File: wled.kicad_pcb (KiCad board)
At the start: 2 copper layers, 61.5 x 28.4 mm, 20 parts, among them J1 PROGRAM_HEADER, J2 LED0, J3 QWIIC, J4 POWER, U1 ESP-12F, U2 AMS1117-3.3

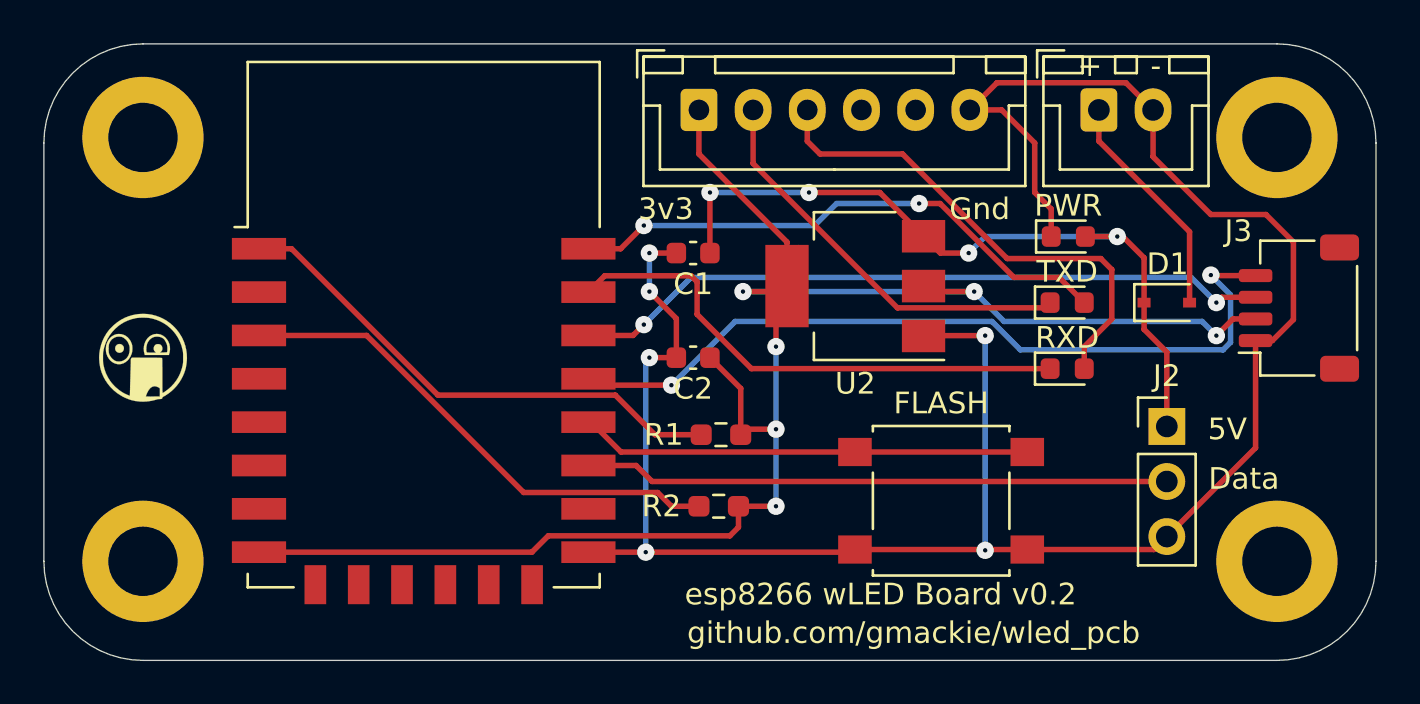
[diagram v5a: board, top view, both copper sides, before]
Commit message: v0.3 (fix LEDs and add reset SW)
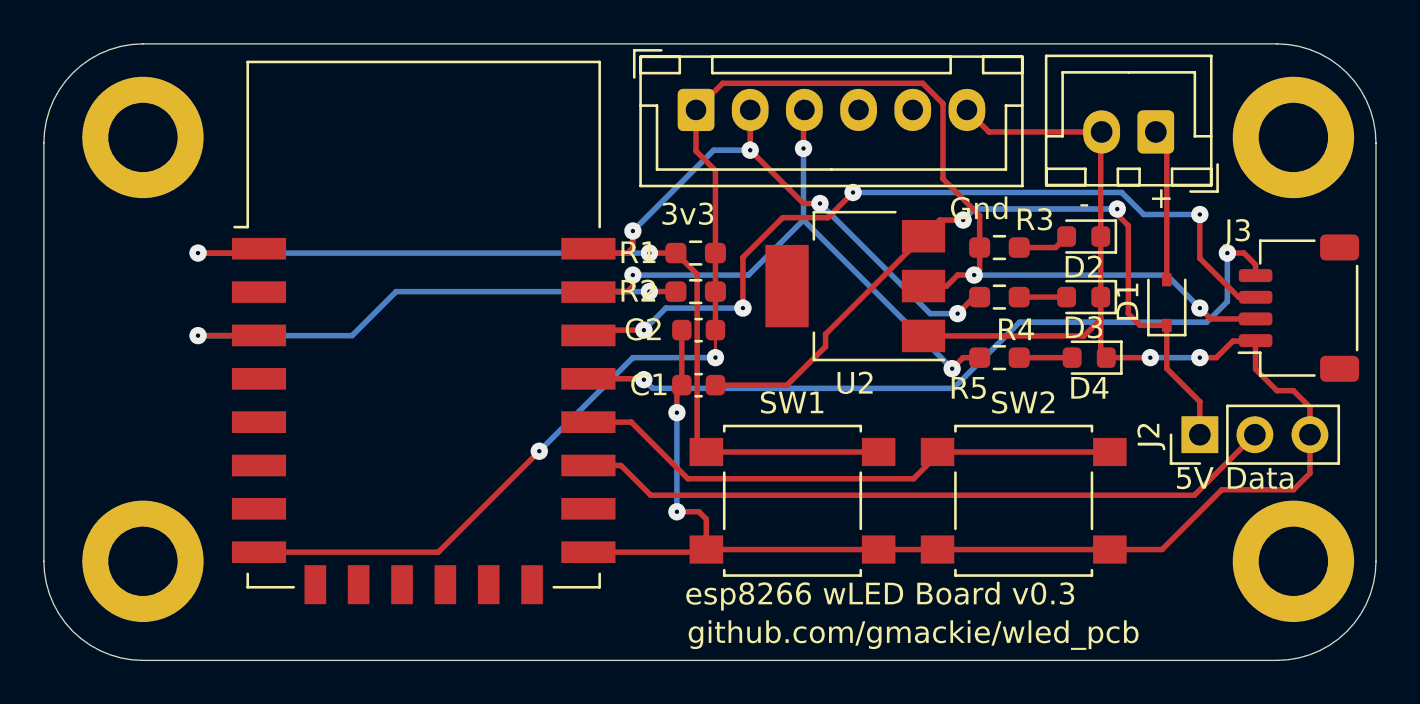
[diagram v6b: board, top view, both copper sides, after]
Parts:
- removed G***: LOGO, wled:bitmap
- added R3: 250, Resistor_SMD:R_0603_1608Metric_Pad0.98x0.95mm_HandSolder, F.Cu at (172.4, 106.2)
- added R4: 10K, Resistor_SMD:R_0603_1608Metric_Pad0.98x0.95mm_HandSolder, F.Cu at (172.4, 108.5)
- added R5: 250, Resistor_SMD:R_0603_1608Metric_Pad0.98x0.95mm_HandSolder, F.Cu at (172.4, 111.3)
- added SW1: RESET, Button_Switch_SMD:SW_SPST_B3S-1000, F.Cu at (162.8, 117.9)
- moved R2 9.96 mm to (158.3, 108.2)
- moved R1 8.46 mm to (158.3, 106.4)
- moved C1 6.10 mm to (158.5, 112.5)
- moved SW2 3.81 mm to (173.5, 117.9)
- moved J4 2.82 mm to (179.6, 100.8), turned to 180 degrees
- moved J2 1.57 mm to (181.6, 114.8), turned to 90 degrees
- moved C2 1.30 mm to (158.5, 110.0)
- moved D4 1.14 mm to (176.5, 111.3), turned to 180 degrees
- moved D3 0.80 mm to (176.3, 108.5), turned to 180 degrees
- moved H3 0.76 mm to (185.9, 101.1)
- moved H4 0.76 mm to (185.9, 120.7)
- moved D2 0.71 mm to (176.3, 105.7), turned to 180 degrees
- moved J1 0.13 mm to (158.4, 99.8)
- turned D1 to 90 degrees
- renumbered PWR to D2, TXD to D3, RXD to D4, FLASH to SW2
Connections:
- D2 pad 2: VDD5V -> Net-(D2-Pad2)
- D3 pad 1: TXD -> GND
- D4 pad 1: Net-(D4-Pad1) -> GND
- D4 pad 2: RXD -> Net-(D4-Pad2)
- U1 pad 21: Net-(D4-Pad1) -> RXD
- U1 pad 22: Net-(D3-Pad2) -> TXD
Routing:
- net Net-(D4-Pad1): track 24.3 -> 0.00 mm
- net Net-(D3-Pad2): track 26.2 -> 2.19 mm, vias 2 -> 0
- net Net-(R1-Pad1): track 24.0 -> 42.7 mm, vias 0 -> 2
- net GND: track 101.7 -> 87.3 mm, vias 6 -> 4
- net TXD: track 19.0 -> 25.8 mm, vias 0 -> 4
- net VDD3V3: track 82.8 -> 76.7 mm, vias 6 -> 4
- net SDA: track 32.5 -> 38.1 mm, vias 2 -> 4
- net DATA: track 27.0 -> 32.5 mm
- net Net-(SW2-Pad1): track 20.8 -> 25.7 mm
- net RXD: track 23.0 -> 27.9 mm, vias 0 -> 3
- net VIN: track 10.6 -> 7.03 mm
- net Net-(D4-Pad2): track 0.00 -> 2.44 mm
- net Net-(D2-Pad2): track 0.00 -> 2.40 mm
- net Net-(R2-Pad1): track 23.6 -> 25.7 mm, vias 0 -> 2
- net SCL: track 37.2 -> 35.6 mm
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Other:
- board text added: "esp8266 wLED Board v0.3"
- board text removed: "esp8266 wLED Board v0.2"
